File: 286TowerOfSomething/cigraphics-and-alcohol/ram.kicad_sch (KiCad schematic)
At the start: 1 part, among them U1 TVGA9000I-3

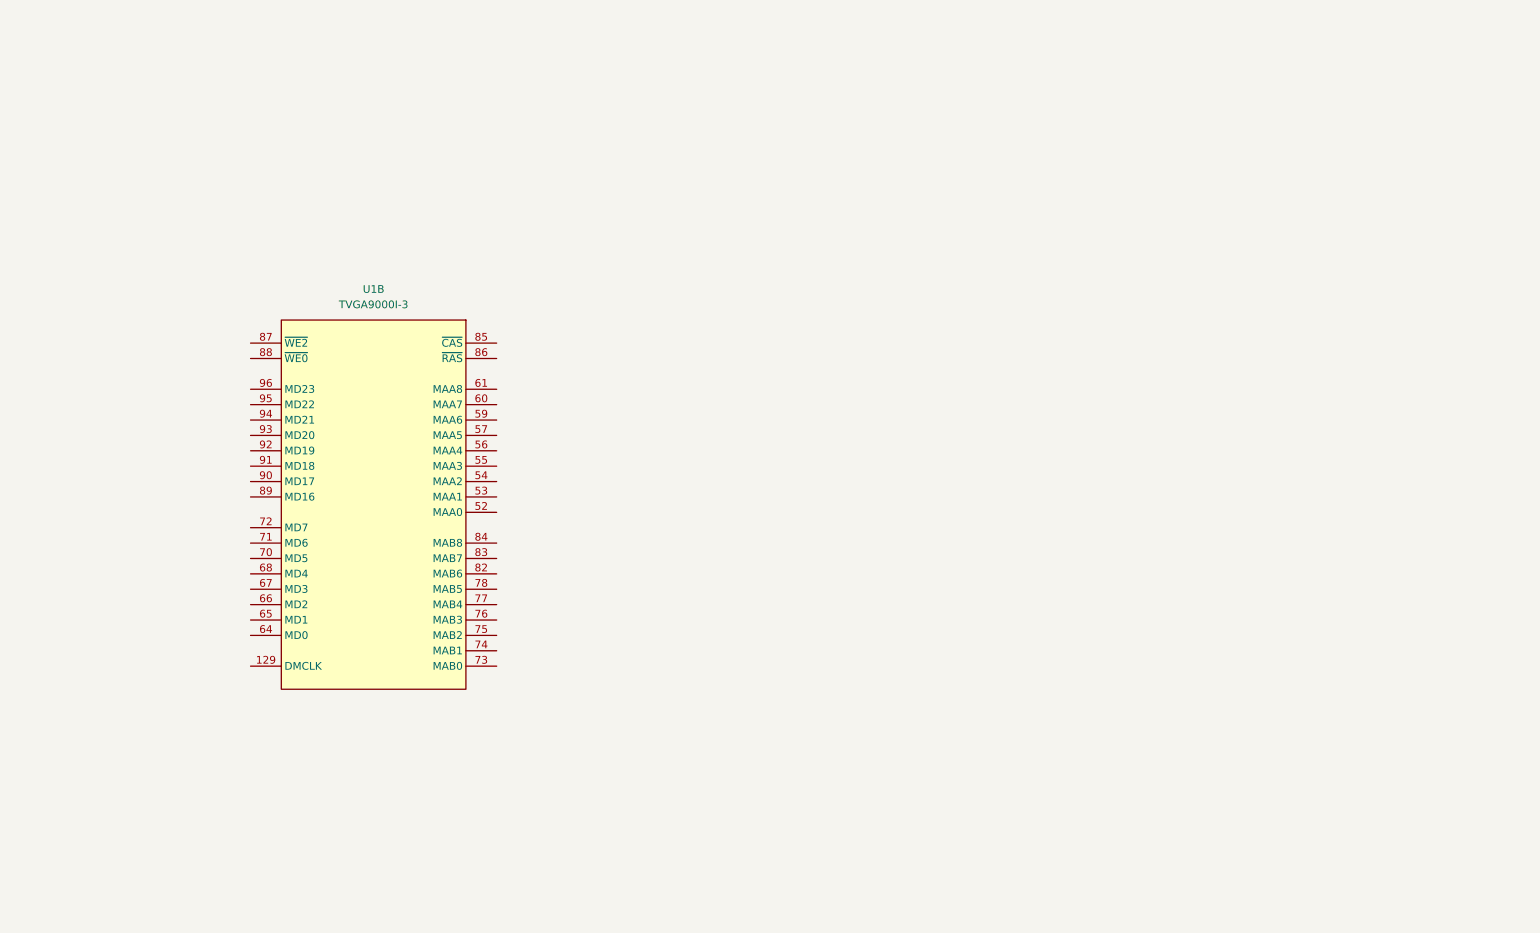
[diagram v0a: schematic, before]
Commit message: Adding RAM to cigraphics-and-alcohol
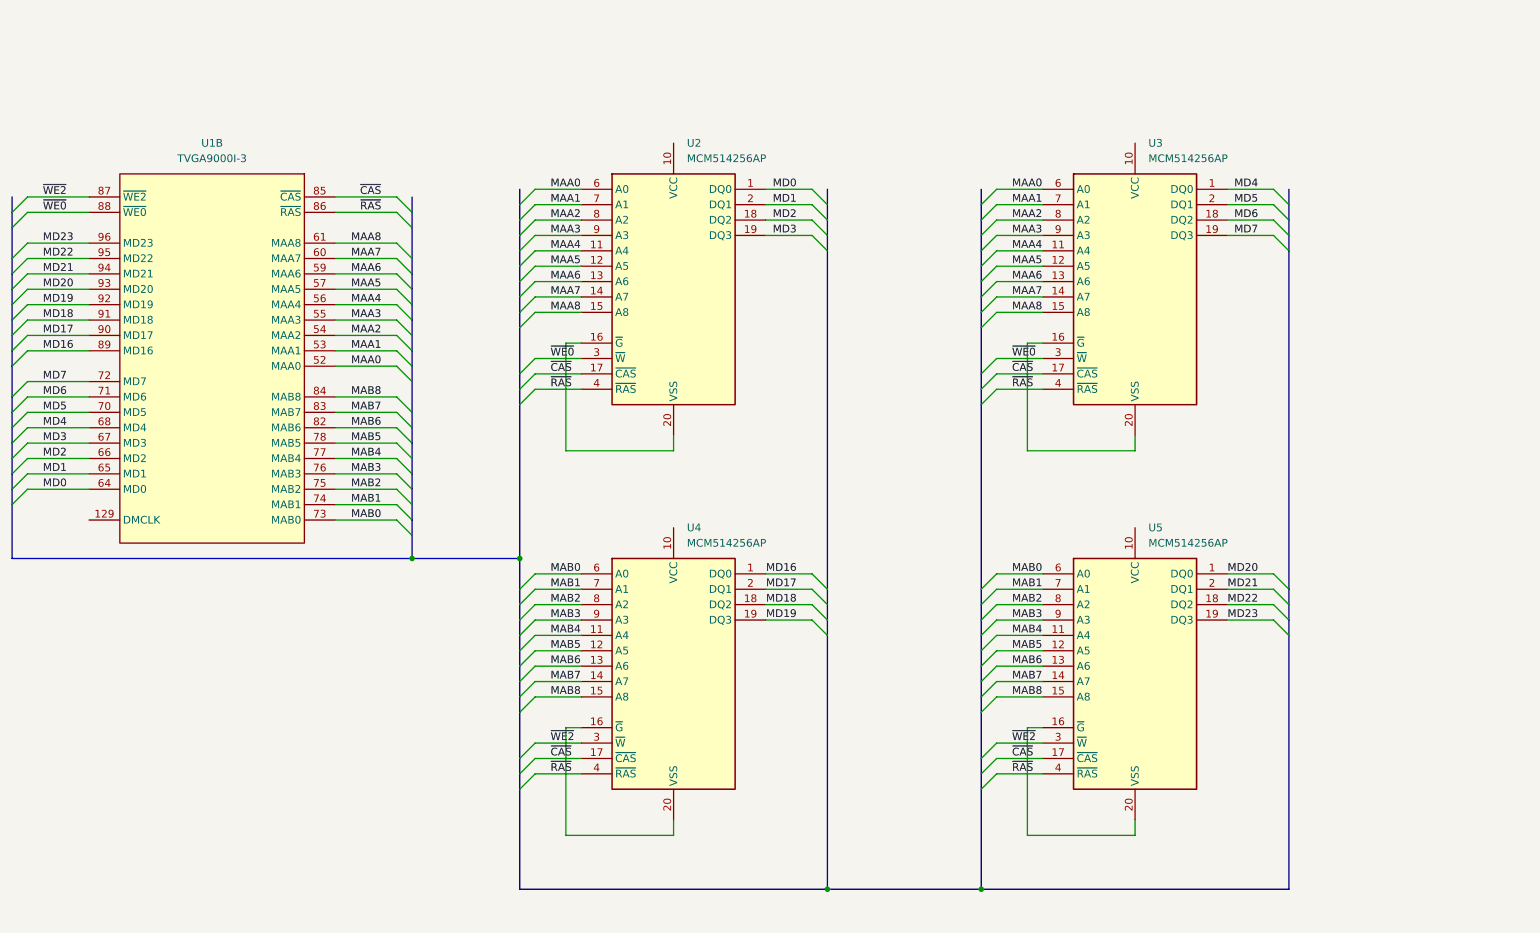
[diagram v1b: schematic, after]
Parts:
- added U2, U3, U4, U5: MCM514256AP, Package_DIP:DIP-20_W7.62mm, symbol pc-parts:MCM514256AP
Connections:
- net MAA0: now reaches U1.52 (MAA0)
- net MAA0: now also U2.6 (A0), U3.6 (A0)
- net MAA1: now reaches U1.53 (MAA1)
- net MAA1: now also U2.7 (A1), U3.7 (A1)
- net MAA2: now reaches U1.54 (MAA2)
- net MAA2: now also U2.8 (A2), U3.8 (A2)
- net MAA3: now reaches U1.55 (MAA3)
- net MAA3: now also U2.9 (A3), U3.9 (A3)
- net MAA4: now reaches U1.56 (MAA4)
- net MAA4: now also U2.11 (A4), U3.11 (A4)
- net MAA5: now reaches U1.57 (MAA5)
- net MAA5: now also U2.12 (A5), U3.12 (A5)
- net MAA6: now reaches U1.59 (MAA6)
- net MAA6: now also U2.13 (A6), U3.13 (A6)
- net MAA7: now reaches U1.60 (MAA7)
- net MAA7: now also U2.14 (A7), U3.14 (A7)
- net MAA8: now reaches U1.61 (MAA8)
- net MAA8: now also U2.15 (A8), U3.15 (A8)
- net MD0: now reaches U1.64 (MD0)
- net MD0: now also U2.1 (DQ0)
- net MD1: now reaches U1.65 (MD1)
- net MD1: now also U2.2 (DQ1)
- net MD2: now reaches U1.66 (MD2)
- net MD2: now also U2.18 (DQ2)
- net MD3: now reaches U1.67 (MD3)
- net MD3: now also U2.19 (DQ3)
- net MD4: now reaches U1.68 (MD4)
- net MD4: now also U3.1 (DQ0)
- net MD5: now reaches U1.70 (MD5)
- net MD5: now also U3.2 (DQ1)
- net MD6: now reaches U1.71 (MD6)
- net MD6: now also U3.18 (DQ2)
- net MD7: now reaches U1.72 (MD7)
- net MD7: now also U3.19 (DQ3)
- net MAB0: now reaches U1.73 (MAB0)
- net MAB0: now also U4.6 (A0), U5.6 (A0)
- net MAB1: now reaches U1.74 (MAB1)
- net MAB1: now also U4.7 (A1), U5.7 (A1)
- net MAB2: now reaches U1.75 (MAB2)
- net MAB2: now also U4.8 (A2), U5.8 (A2)
- net MAB3: now reaches U1.76 (MAB3)
- net MAB3: now also U4.9 (A3), U5.9 (A3)
- net MAB4: now reaches U1.77 (MAB4)
- net MAB4: now also U4.11 (A4), U5.11 (A4)
- net MAB5: now reaches U1.78 (MAB5)
- net MAB5: now also U4.12 (A5), U5.12 (A5)
- net MAB6: now reaches U1.82 (MAB6)
- net MAB6: now also U4.13 (A6), U5.13 (A6)
- net MAB7: now reaches U1.83 (MAB7)
- net MAB7: now also U4.14 (A7), U5.14 (A7)
- net MAB8: now reaches U1.84 (MAB8)
- net MAB8: now also U4.15 (A8), U5.15 (A8)
- net ~{CAS}: now reaches U1.85 (~{CAS})
- net ~{CAS}: now also U2.17 (~{CAS}), U3.17 (~{CAS}), U4.17 (~{CAS}), U5.17 (~{CAS})
- net ~{RAS}: now reaches U1.86 (~{RAS})
- net ~{RAS}: now also U2.4 (~{RAS}), U3.4 (~{RAS}), U4.4 (~{RAS}), U5.4 (~{RAS})
- net ~{WE2}: now reaches U1.87 (~{WE2})
- net ~{WE2}: now also U4.3 (~{W}), U5.3 (~{W})
- net ~{WE0}: now reaches U1.88 (~{WE0})
- net ~{WE0}: now also U2.3 (~{W}), U3.3 (~{W})
- net MD16: now reaches U1.89 (MD16)
- net MD16: now also U4.1 (DQ0)
- net MD17: now reaches U1.90 (MD17)
- net MD17: now also U4.2 (DQ1)
- net MD18: now reaches U1.91 (MD18)
- net MD18: now also U4.18 (DQ2)
- net MD19: now reaches U1.92 (MD19)
- net MD19: now also U4.19 (DQ3)
- net MD20: now reaches U1.93 (MD20)
- net MD20: now also U5.1 (DQ0)
- net MD21: now reaches U1.94 (MD21)
- net MD21: now also U5.2 (DQ1)
- net MD22: now reaches U1.95 (MD22)
- net MD22: now also U5.18 (DQ2)
- net MD23: now reaches U1.96 (MD23)
- net MD23: now also U5.19 (DQ3)
- new net: U5.16 (~{G}), U5.20 (VSS)
- new net: U4.16 (~{G}), U4.20 (VSS)
- new net: U2.16 (~{G}), U2.20 (VSS)
- new net: U3.16 (~{G}), U3.20 (VSS)
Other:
- moved on the sheet: U1B

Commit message: Almost finished schematic for cigraphics-and-alcohol
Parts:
- added C1, C2, C3, C4: 100n, Capacitor_SMD:C_0603_1608Metric_Pad1.08x0.95mm_HandSolder, symbol Device:C
- added R13, R14, R15: 4.7K, Resistor_SMD:R_0603_1608Metric_Pad0.98x0.95mm_HandSolder, symbol Device:R
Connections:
- net MD2: now also R13.1, R13.2
- net MD3: now also R14.1
- net MD7: now also R15.1, R15.2
- net +5V: now reaches U5.10 (VCC)
- net +5V: now also U2.10 (VCC), U3.10 (VCC), U4.10 (VCC), C1.1, C2.1, C3.1, C4.1
- net GND: now reaches U5.16 (~{G}), U5.20 (VSS)
- net GND: now also U2.16 (~{G}), U2.20 (VSS), U3.16 (~{G}), U3.20 (VSS), U4.16 (~{G}), U4.20 (VSS), C1.2, C2.2, C3.2, C4.2, R14.2
- no-connect marks 0 -> 1

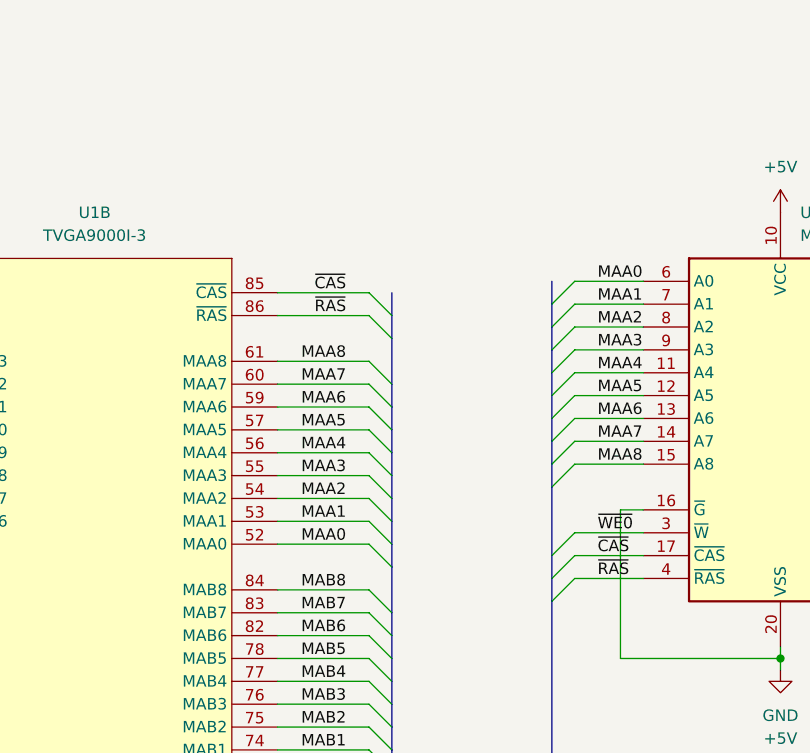
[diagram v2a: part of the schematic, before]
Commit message: Adding datasheet for DRAM for video card, and fixing CAS and RAS on video card
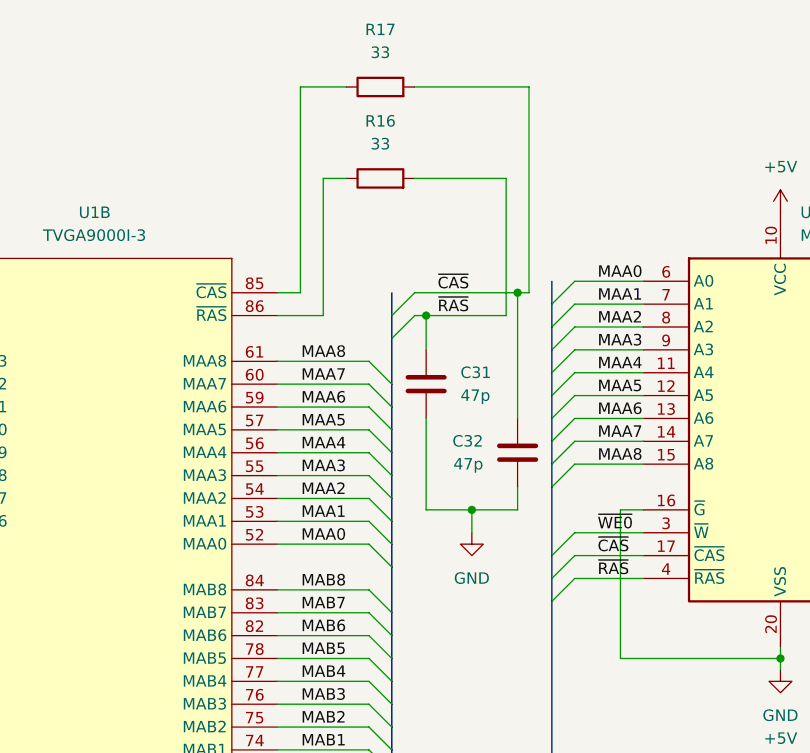
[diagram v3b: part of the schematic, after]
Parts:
- added C31, C32: 47p, Capacitor_SMD:C_0603_1608Metric_Pad1.08x0.95mm_HandSolder, symbol Device:C
- added R16, R17: 33, Resistor_SMD:R_0603_1608Metric_Pad0.98x0.95mm_HandSolder, symbol Device:R
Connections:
- net GND: now also C31.2, C32.2
- net ~{CAS}: now also C32.1, R17.2; no longer U1.85 (~{CAS})
- net ~{RAS}: now also C31.1, R16.2; no longer U1.86 (~{RAS})
- new net: R17.1, U1.85 (~{CAS})
- new net: R16.1, U1.86 (~{RAS})
